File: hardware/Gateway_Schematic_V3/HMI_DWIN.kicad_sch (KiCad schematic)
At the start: 1 part, among them J2 Conn_01x04_Pin

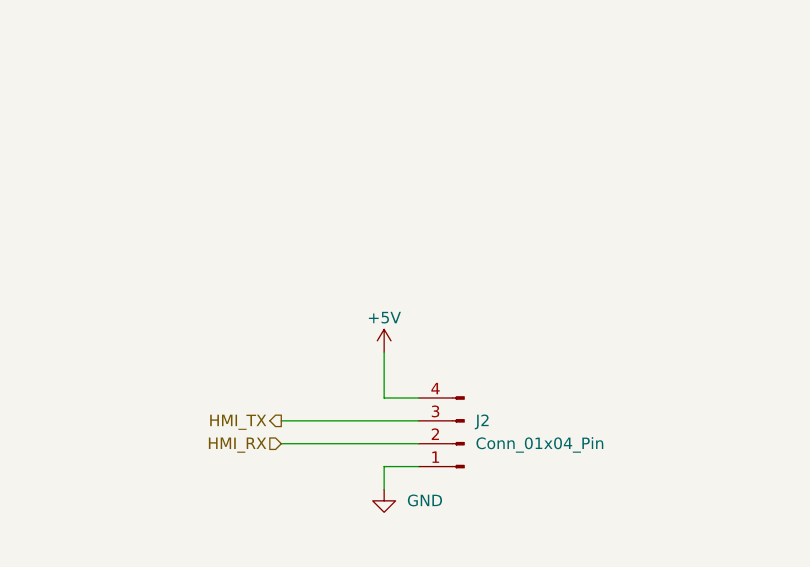
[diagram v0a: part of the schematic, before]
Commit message: Update PCB Layout after review 27/3/2026
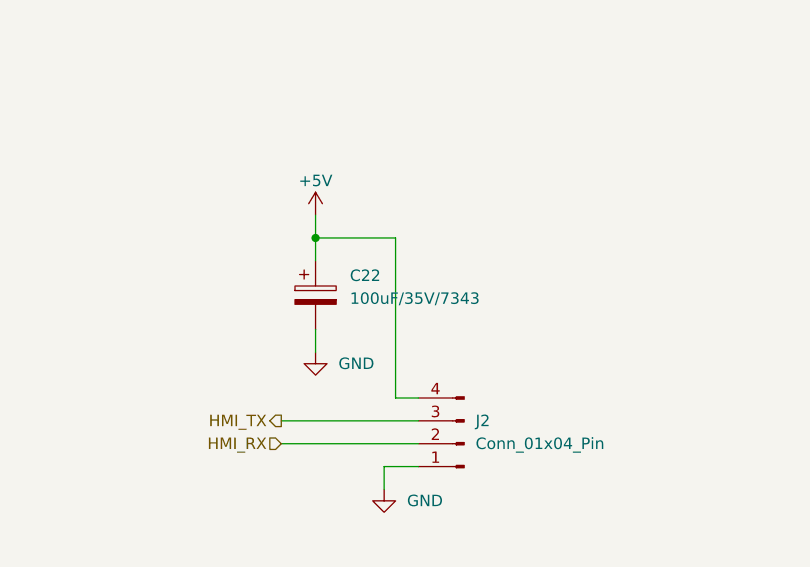
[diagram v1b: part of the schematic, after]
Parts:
- added C22: 100uF/35V/7343, Capacitor_Tantalum_SMD:CP_EIA-7132-28_AVX-C_Pad2.72x3.50mm_HandSolder, symbol Device:C_Polarized
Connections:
- net +5V: now also C22.1
- net GND: now also C22.2
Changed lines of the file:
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@@
 		)
 	)
-	(wire
-		(pts
-			(xy 139.7 87.63) (xy 139.7 82.55)
-		)
-		(stroke
-			(width 0)
-			(type default)
-		)
+	(junction
+		(at 132.08 69.85)
+		(diameter 0)
+		(color 0 0 0 0)
 	)
 	(wire
@@
 	(wire
 		(pts
+			(xy 132.08 72.39) (xy 132.08 69.85)
+		)
+		(stroke
+			(width 0)
+			(type default)
+		)
+	)
+	(wire
+		(pts
 			(xy 128.27 90.17) (xy 143.51 90.17)
 		)
@@
 	(wire
 		(pts
-			(xy 143.51 87.63) (xy 139.7 87.63)
+			(xy 140.97 69.85) (xy 132.08 69.85)
+		)
+		(stroke
+			(width 0)
+			(type default)
+		)
+	)
+	(wire
+		(pts
+			(xy 143.51 87.63) (xy 140.97 87.63)
+		)
+		(stroke
+			(width 0)
+			(type default)
+		)
+	)
+	(wire
+		(pts
+			(xy 132.08 80.01) (xy 132.08 82.55)
+		)
+		(stroke
+			(width 0)
+			(type default)
+		)
+	)
+	(wire
+		(pts
+			(xy 132.08 69.85) (xy 132.08 67.31)
+		)
+		(stroke
+			(width 0)
+			(type default)
+		)
+	)
+	(wire
+		(pts
+			(xy 140.97 87.63) (xy 140.97 69.85)
 		)
 		(stroke
@@
 	)
 	(symbol
+		(lib_id "Device:C_Polarized")
+		(at 132.08 76.2 0)
+		(unit 1)
+		(exclude_from_sim no)
+		(in_bom yes)
+		(on_board yes)
+		(dnp no)
+		(fields_autoplaced yes)
+		(property "Reference" "C22"
+			(at 135.89 74.0409 0)
+			(effects
+				(font
+					(size 1.27 1.27)
+				)
+				(justify left)
+			)
+		)
+		(property "Value" "100uF/35V/7343"
+			(at 135.89 76.5809 0)
+			(effects
+				(font
+					(size 1.27 1.27)
+				)
+				(justify left)
+			)
+		)
+		(property "Footprint" "Capacitor_Tantalum_SMD:CP_EIA-7132-28_AVX-C_Pad2.72x3.50mm_HandSolder"
+			(at 133.0452 80.01 0)
+			(effects
+				(font
+					(size 1.27 1.27)
+				)
+				(hide yes)
+			)
+		)
+		(property "Datasheet" "~"
+			(at 132.08 76.2 0)
+			(effects
+				(font
+					(size 1.27 1.27)
+				)
+				(hide yes)
+			)
+		)
+		(property "Description" "Polarized capacitor"
+			(at 132.08 76.2 0)
+			(effects
+				(font
+					(size 1.27 1.27)
+				)
+				(hide yes)
+			)
+		)
+		(pin "1"
+		)
+		(pin "2"
+		)
+		(instances
+			(project ""
+				(path "/08b065f5-231d-43cb-bb9e-87dca43beac9/b068e736-77a3-4da7-b7df-319407e96c28"
+					(reference "C22")
+					(unit 1)
+				)
+			)
+		)
+	)
+	(symbol
 		(lib_id "power:GND")
 		(at 139.7 97.79 0)
@@
 	(symbol
 		(lib_id "power:+5V")
-		(at 139.7 82.55 0)
+		(at 132.08 67.31 0)
 		(unit 1)
 		(exclude_from_sim no)
@@
 		(dnp no)
 		(property "Reference" "#PWR097"
-			(at 139.7 86.36 0)
+			(at 132.08 71.12 0)
 			(effects
 				(font
@@
 		)
 		(property "Value" "+5V"
-			(at 139.7 78.74 0)
+			(at 132.08 63.5 0)
 			(effects
 				(font
@@
 		)
 		(property "Footprint" ""
-			(at 139.7 82.55 0)
+			(at 132.08 67.31 0)
 			(effects
 				(font
@@
 		)
 		(property "Datasheet" ""
-			(at 139.7 82.55 0)
+			(at 132.08 67.31 0)
 			(effects
 				(font
@@
 		)
 		(property "Description" "Power symbol creates a global label with name \"+5V\""
-			(at 139.7 82.55 0)
+			(at 132.08 67.31 0)
 			(effects
 				(font
@@
 					(unit 1)
 				)
+			)
+		)
+	)
+	(symbol
+		(lib_id "power:GND")
+		(at 132.08 82.55 0)
+		(unit 1)
+		(exclude_from_sim no)
+		(in_bom yes)
+		(on_board yes)
+		(dnp no)
+		(fields_autoplaced yes)
+		(property "Reference" "#PWR025"
+			(at 132.08 88.9 0)
+			(effects
+				(font
+					(size 1.27 1.27)
+				)
+				(hide yes)
+			)
+		)
+		(property "Value" "GND"
+			(at 134.62 83.8199 0)
+			(effects
+				(font
+					(size 1.27 1.27)
+				)
+				(justify left)
+			)
+		)
+		(property "Footprint" ""
+			(at 132.08 82.55 0)
+			(effects
+				(font
+					(size 1.27 1.27)
+				)
+				(hide yes)
+			)
+		)
+		(property "Datasheet" ""
+			(at 132.08 82.55 0)
+			(effects
+				(font
+					(size 1.27 1.27)
+				)
+				(hide yes)
+			)
+		)
+		(property "Description" "Power symbol creates a global label with name \"GND\" , ground"
+			(at 132.08 82.55 0)
+			(effects
+				(font
+					(size 1.27 1.27)
+				)
+				(hide yes)
+			)
+		)
+		(pin "1"
+		)
+		(instances
+			(project "Gateway_Schematic_V3"
+				(path "/08b065f5-231d-43cb-bb9e-87dca43beac9/b068e736-77a3-4da7-b7df-319407e96c28"
+					(reference "#PWR025")
+					(unit 1)
+				)
